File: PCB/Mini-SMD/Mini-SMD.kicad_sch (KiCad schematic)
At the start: 26 parts, among them J1 Daisy port out, J2 2-pin header, J3 ICSP_ISP6, J4 Daisy port in, K1 HYC77-TF09-200, U1 PC817C-S, U2 ATmega328P-AU, U3 SE5218, U4 TXB0104PWR, Y1 Resonator_GND2

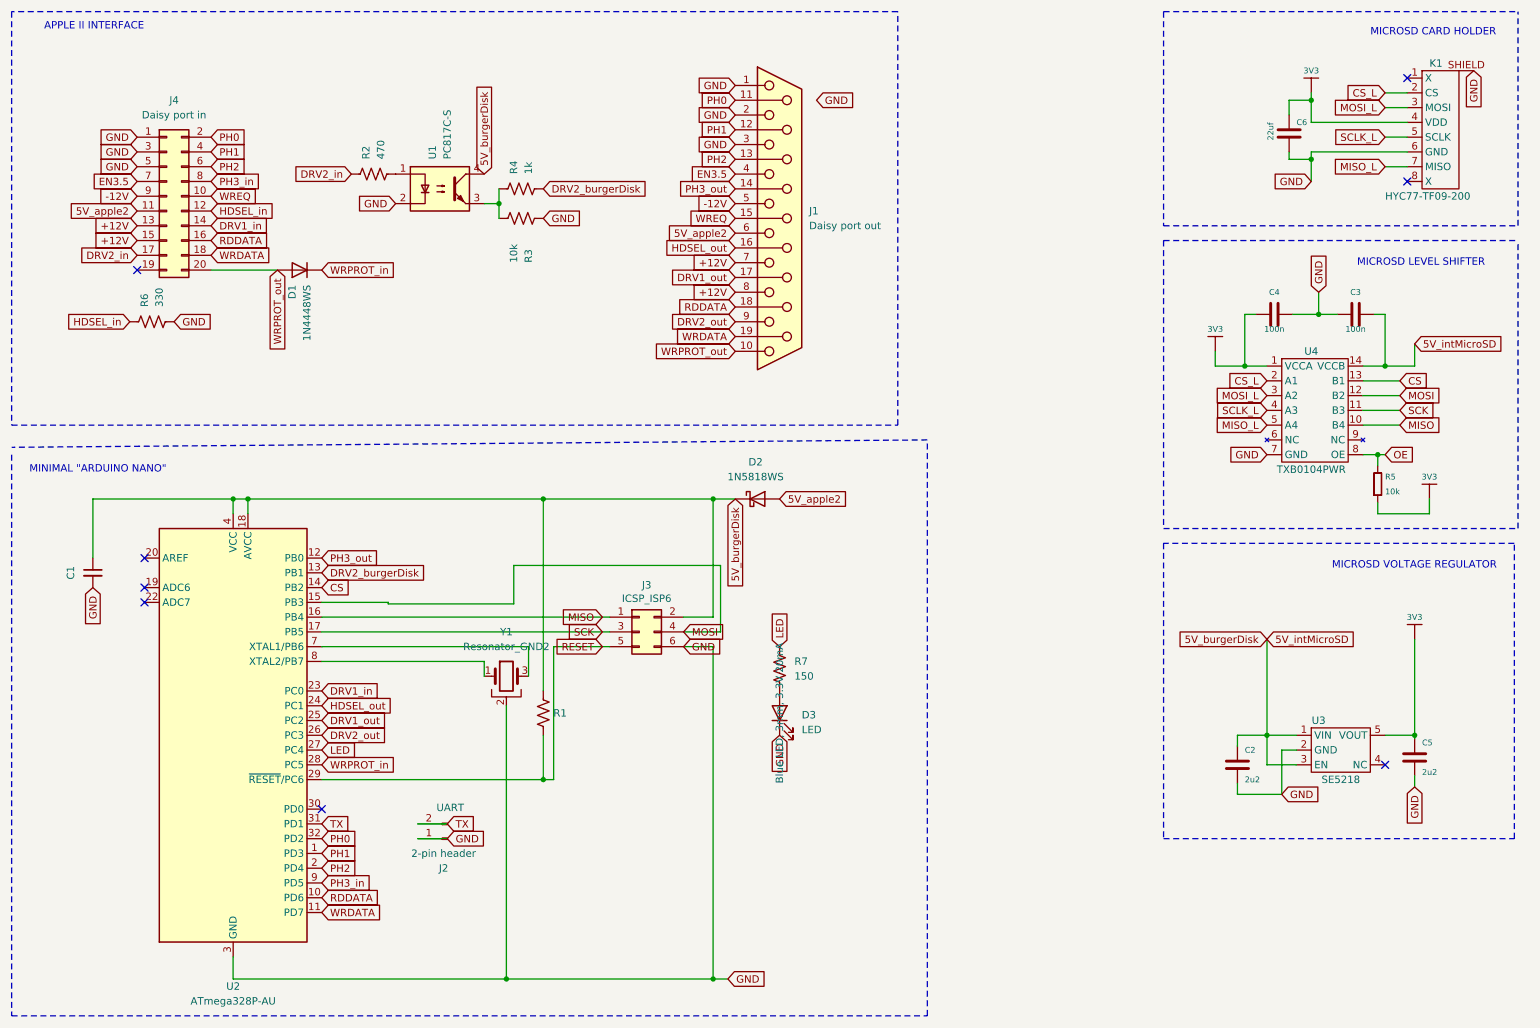
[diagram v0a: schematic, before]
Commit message: Make PCBs closer to one another
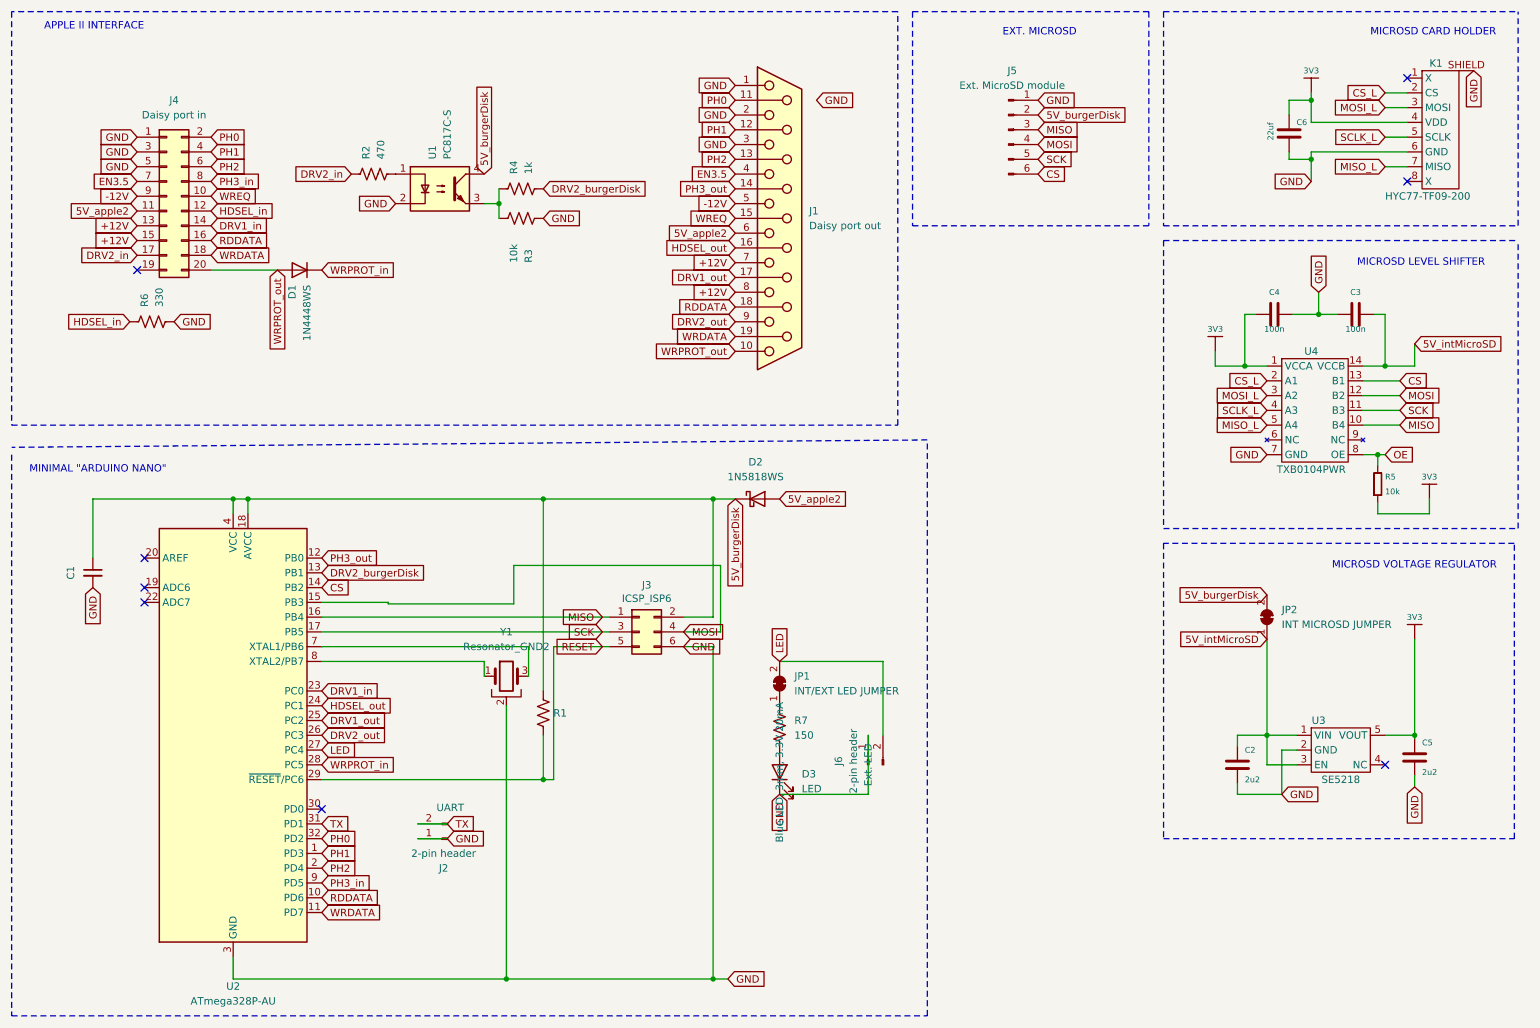
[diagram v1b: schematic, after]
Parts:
- added J5: Ext. MicroSD module, Connector_PinHeader_2.54mm:PinHeader_1x06_P2.54mm_Vertical, symbol Connector:Conn_01x06_Pin
- added J6: 2-pin header, Connector_PinHeader_2.54mm:PinHeader_1x02_P2.54mm_Vertical, symbol Connector:Conn_01x02_Pin
- added JP1: INT/EXT LED JUMPER, Jumper:SolderJumper-2_P1.3mm_Bridged_Pad1.0x1.5mm, symbol Jumper:SolderJumper_2_Bridged
- added JP2: INT MICROSD JUMPER, Jumper:SolderJumper-2_P1.3mm_Bridged_Pad1.0x1.5mm, symbol Jumper:SolderJumper_2_Bridged
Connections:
- net 5V_burgerDisk: now also J5.2 (Pin_2), JP2.2 (B); no longer C2.2, C3.2, U3.1 (VIN), U3.3 (EN), U4.14 (VCCB)
- net CS: now also J5.6 (Pin_6)
- net GND: now also J5.1 (Pin_1), J6.1 (+5V)
- net LED: now also J6.2 (GND), JP1.2 (B); no longer R7.2
- net MISO: now also J5.3 (Pin_3)
- net MOSI: now also J5.4 (Pin_4)
- net SCK: now also J5.5 (Pin_5)
- new net: JP1.1 (A), R7.2
- new net 5V_intMicroSD: C2.2, C3.2, JP2.1 (A), U3.1 (VIN), U3.3 (EN), U4.14 (VCCB)
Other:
- note added: "EXT. MICROSD"
- moved on the sheet: D3, R7

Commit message: Move to bigger pads for diodes
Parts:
- D1: footprint Diode_SMD:D_SOD-323F -> Diode_SMD:D_SOD-323_HandSoldering
- D2: footprint Diode_SMD:D_SOD-323 -> Diode_SMD:D_SOD-323_HandSoldering
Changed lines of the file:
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@@
 			)
 		)
-		(property "Footprint" "Diode_SMD:D_SOD-323F"
+		(property "Footprint" "Diode_SMD:D_SOD-323_HandSoldering"
 			(at 67.31 61.595 0)
 			(effects
@@
 			)
 		)
-		(property "Footprint" "Diode_SMD:D_SOD-323"
+		(property "Footprint" "Diode_SMD:D_SOD-323_HandSoldering"
 			(at 146.05 109.855 0)
 			(effects
